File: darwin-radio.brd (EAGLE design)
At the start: 110 x 72.9 mm, 42 parts, among them J1 505110-1692, J2 505110-1692, J3 M55-6102042R, Q2 NDS8434, U1 ATWINC, U6 MCP7384X

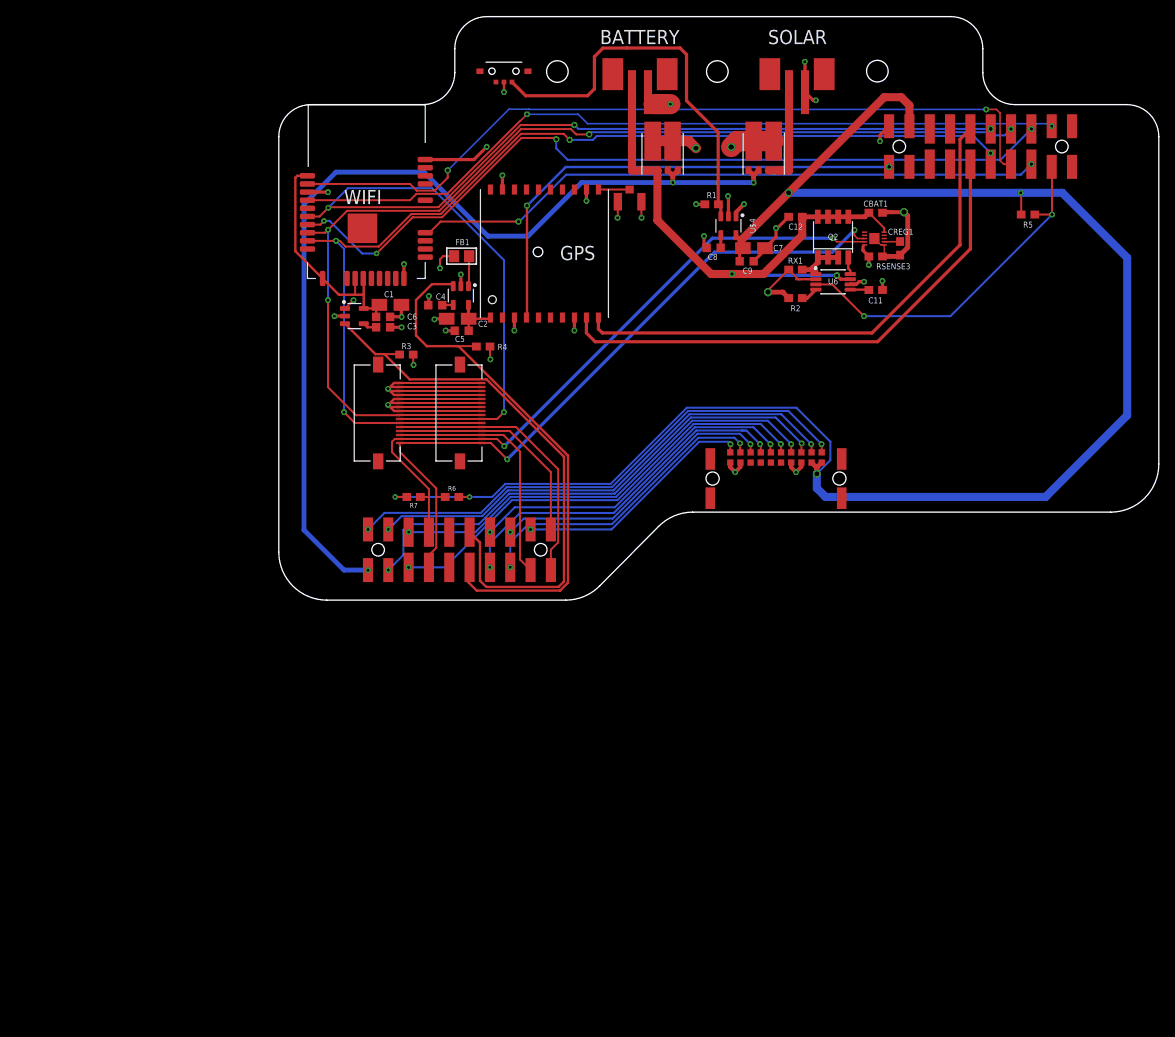
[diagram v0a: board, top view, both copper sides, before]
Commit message: Added external button header. added mounting point for single 'backpack' module. Panelized. PA1.
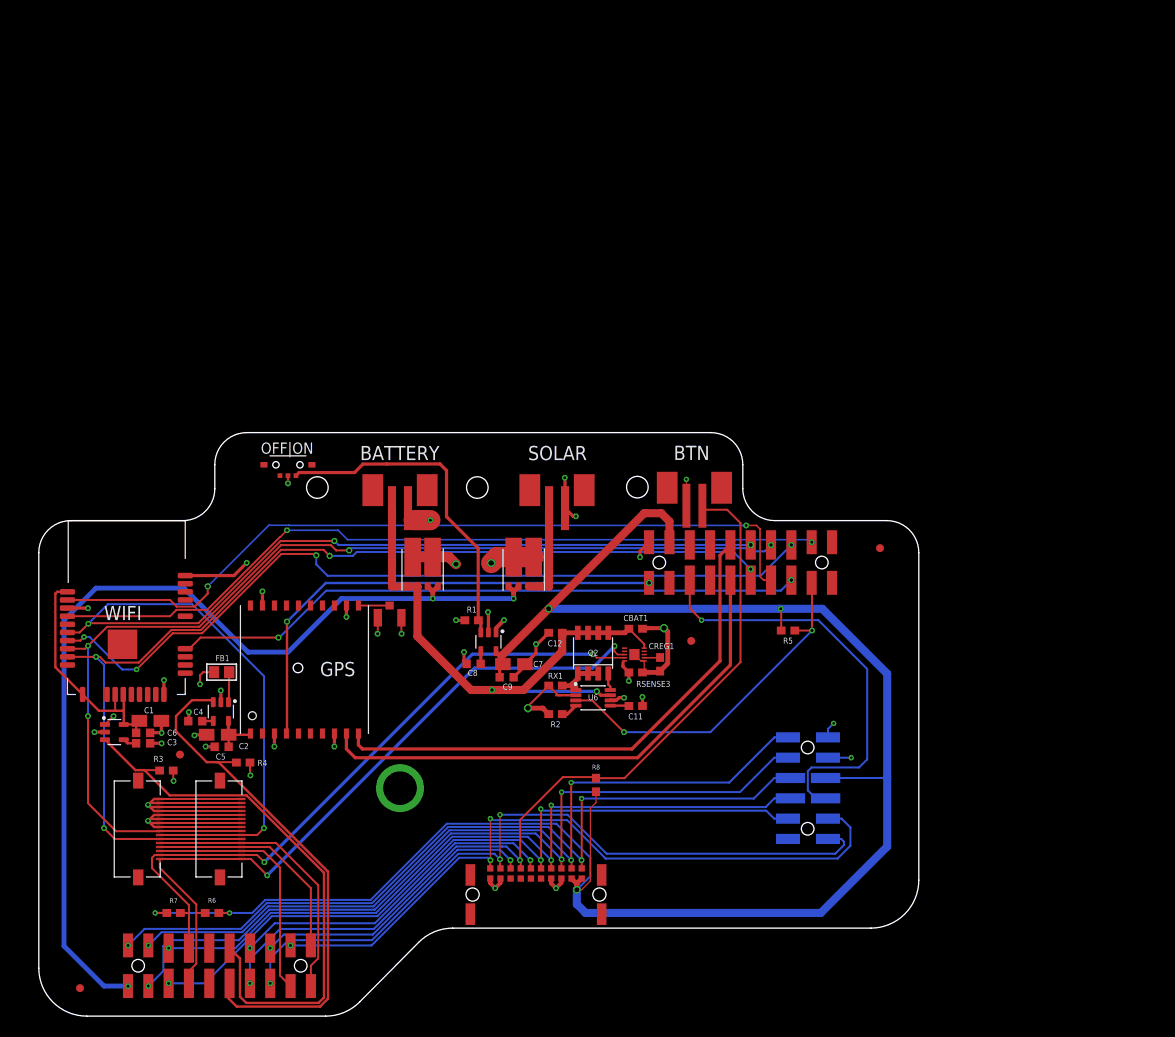
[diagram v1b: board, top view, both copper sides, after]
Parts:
- added FID1, FID2, FID3, FID4: FIDUCIAL_1MM, microbuilder:FIDUCIAL_1MM
- added R8: 100k, SparkFun-Resistors:0603
- added U$8: 2X6-HEADERSDS, Conservify:12PH
- added U$9: B2B-PH-SM4-TB, Conservify:B2B-PH-SM4-TB
- moved C12 60.0 mm to (65.4, 48.4)
- moved C7 60.0 mm to (60.2, 44.5)
- moved C9 60.0 mm to (59.3, 42.9)
- moved R6 60.0 mm to (22.5, 13.4)
- moved R7 60.0 mm to (17.7, 13.4)
- moved U$3 60.0 mm to (10.3, 36.0)
- moved U$4 60.0 mm to (57.1, 47.3)
- moved U6 60.0 mm to (70.1, 40.3)
- moved C1 60.0 mm to (14.8, 37.4)
- moved C11 60.0 mm to (75.5, 39.3)
- moved C3 60.0 mm to (13.9, 34.6)
- moved C6 60.0 mm to (13.9, 35.9)
- moved C8 60.0 mm to (55.2, 44.5)
- moved CBAT1 60.0 mm to (75.5, 48.9)
- moved D1 60.0 mm to (48.8, 53.7)
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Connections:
- net MOD_G12 renamed CHARGING
- net MOD_G3 renamed HOTSWAP_INT
- net MOD_G6 renamed GPS_ENABLE
- net MOD_G7 renamed WIFI_ENABLE
- removed net MOD_G1: J3.P1, LOWER1.PIN2
- removed net MOD_G4: J3.P4, LOWER1.PIN17
- removed net X1: UPPER1.PIN3
- new net BACKPACK_ENABLE: U$8.4, UPPER1.PIN3
- new net EEPROM_PROT: J3.P1, LOWER1.PIN2, U$8.5
- new net PIN7: U$8.7
- new net XBTN: J3.P4, LOWER1.PIN17, R8.2, U$9.-
- net 3V3: now also R8.1, U$8.3
- net GND: now also U$8.2, U$9.+
- net MOD_G2: now also U$8.6
- net MOD_MISO: now also U$8.10
- net MOD_MOSI: now also U$8.11
- net MOD_SCK: now also U$8.12
- net MOD_SCL: now also U$8.8
- net MOD_SDA: now also U$8.9
- net UNREG: now also U$8.1
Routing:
- net XBTN: track 0.00 -> 108.3 mm, vias 0 -> 2
- net EEPROM_PROT: track 0.00 -> 89.1 mm, vias 0 -> 3
- net MOD_G2: track 38.7 -> 92.3 mm, vias 2 -> 3
- net BACKPACK_ENABLE: track 0.00 -> 53.2 mm, vias 0 -> 1
- net MOD_G4: track 44.4 -> 0.00 mm, vias 2 -> 0
- net MOD_SCK: track 61.4 -> 100.6 mm, vias 2 -> 3
- net MOD_MOSI: track 63.9 -> 102.4 mm, vias 2 -> 3
- net MOD_SCL: track 56.0 -> 93.9 mm, vias 2 -> 3
- net MOD_SDA: track 55.8 -> 93.2 mm, vias 2 -> 3
- net MOD_MISO: track 65.6 -> 100.5 mm, vias 2 -> 3
- net MOD_G1: track 30.7 -> 0.00 mm, vias 2 -> 0
- net 3V3: track 220.3 -> 242.7 mm
- net N$8: track 49.7 -> 41.8 mm
- net GND: track 125.3 -> 131.5 mm, vias 30 -> 32
- net GPS_ENABLE: track 69.8 -> 67.4 mm
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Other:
- board text added: "BTN"
- board text added: "OFF|ON"

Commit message: Cleanup.
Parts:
- removed J1, J2: 505110-1692, Conservify:505110-1692
- removed J3: M55-6102042R, Conservify:M55-6102042R
- removed U$6, U$7, U$9: B2B-PH-SM4-TB, Conservify:B2B-PH-SM4-TB
- removed U$8: 2X6-HEADERSDS, Conservify:12PH
- added BACKPACK: 2X6-HEADERSDS, Conservify:12PH
- added BACKPLANE: M55-6102042R, Conservify:M55-6102042R
- added BAT-JST, BTN-JST, SOLAR-JST: B2B-PH-SM4-TB, Conservify:B2B-PH-SM4-TB
- added FFC1, FFC2: 505110-1692, Conservify:505110-1692
- C3, C4, C8: value (none) -> 470pf
- moved U$5 4.88 mm to (27.1, 68.9)
- moved FID3 0.99 mm to (81.5, 46.9)
- moved C2 0.99 mm to (22.4, 35.2)
- moved C4 0.99 mm to (19.6, 36.9)
- moved C5 0.99 mm to (22.9, 33.7)
- moved C7 0.99 mm to (59.4, 44.0)
- moved C8 0.99 mm to (54.4, 44.0)
- moved C9 0.99 mm to (58.5, 42.4)
- moved D3 0.99 mm to (60.6, 53.2)
- moved FID4 0.99 mm to (17.6, 32.7)
- moved LOWER1 0.99 mm to (34.0, 8.50)
- moved R1 0.99 mm to (54.1, 49.5)
- moved R3 0.99 mm to (15.9, 30.7)
- moved R6 0.99 mm to (21.6, 12.9)
- moved U$1 0.99 mm to (33.2, 43.3)
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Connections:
- net 3V3: now also BACKPACK.3, BACKPLANE.P11, BACKPLANE.P12; no longer J3.P11, J3.P12, U$8.3
- net BACKPACK_ENABLE: now also BACKPACK.4; no longer U$8.4
- net BAT+: now also BAT-JST.+; no longer U$7.+
- net BAT-: now also BAT-JST.-; no longer U$7.-
- net EEPROM_PROT: now also BACKPACK.5, BACKPLANE.P1; no longer J3.P1, U$8.5
- net GND: now also BACKPACK.2, BACKPLANE.P19, BACKPLANE.P20, BTN-JST.+, FFC1.1, FFC1.2, FFC1.3, FFC1.4, FFC2.1, FFC2.2, FFC2.3, FFC2.4, SOLAR-JST.-; no longer J1.1, J1.2, J1.3, J1.4, J2.1, J2.2, J2.3, J2.4, J3.P19, J3.P20, U$6.-, U$8.2, U$9.+
- net HOTSWAP_INT: now also BACKPLANE.P3; no longer J3.P3
- net MOD_G0: now also FFC1.13, FFC2.13; no longer J1.13, J2.13
- net MOD_G13: now also FFC1.14, FFC2.14; no longer J1.14, J2.14
- net MOD_G14: now also FFC1.12, FFC2.12; no longer J1.12, J2.12
- net MOD_G2: now also BACKPACK.6, BACKPLANE.P2; no longer J3.P2, U$8.6
- net MOD_G5: now also BACKPLANE.P5; no longer J3.P5
- net MOD_MISO: now also BACKPACK.10, BACKPLANE.P10; no longer J3.P10, U$8.10
- net MOD_MOSI: now also BACKPACK.11, BACKPLANE.P8; no longer J3.P8, U$8.11
- net MOD_SCK: now also BACKPACK.12, BACKPLANE.P9; no longer J3.P9, U$8.12
- net MOD_SCL: now also BACKPACK.8, BACKPLANE.P6; no longer J3.P6, U$8.8
- net MOD_SDA: now also BACKPACK.9, BACKPLANE.P7; no longer J3.P7, U$8.9
- net PIN7: now also BACKPACK.7; no longer U$8.7
- net RADIO_MISO: now also FFC1.9, FFC2.9; no longer J1.9, J2.9
- net RADIO_MOSI: now also FFC1.10, FFC2.10; no longer J1.10, J2.10
- net RADIO_SCK: now also FFC1.11, FFC2.11; no longer J1.11, J2.11
- net RAD_SCL: now also FFC1.16, FFC2.16; no longer J1.16, J2.16
- net RAD_SDA: now also FFC1.15, FFC2.15; no longer J1.15, J2.15
- net SOL+: now also SOLAR-JST.+; no longer U$6.+
- net UNREG: now also BACKPACK.1, BACKPLANE.P13, BACKPLANE.P14, FFC1.5, FFC1.6, FFC1.7, FFC1.8, FFC2.5, FFC2.6, FFC2.7, FFC2.8; no longer J1.5, J1.6, J1.7, J1.8, J2.5, J2.6, J2.7, J2.8, J3.P13, J3.P14, U$8.1
- net XBTN: now also BACKPLANE.P4, BTN-JST.-; no longer J3.P4, U$9.-
- net XX1: now also BACKPLANE.P18; no longer J3.P18
- net XX2: now also BACKPLANE.P17; no longer J3.P17
- net XX3: now also BACKPLANE.P16; no longer J3.P16
- net XX4: now also BACKPLANE.P15; no longer J3.P15
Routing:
- net N$8: track 41.8 -> 47.5 mm
- net GPS_TX: track 66.4 -> 64.5 mm
- net GPS_RX: track 65.8 -> 64.1 mm
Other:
- board size 110 x 72.9 mm -> 110 x 73 mm

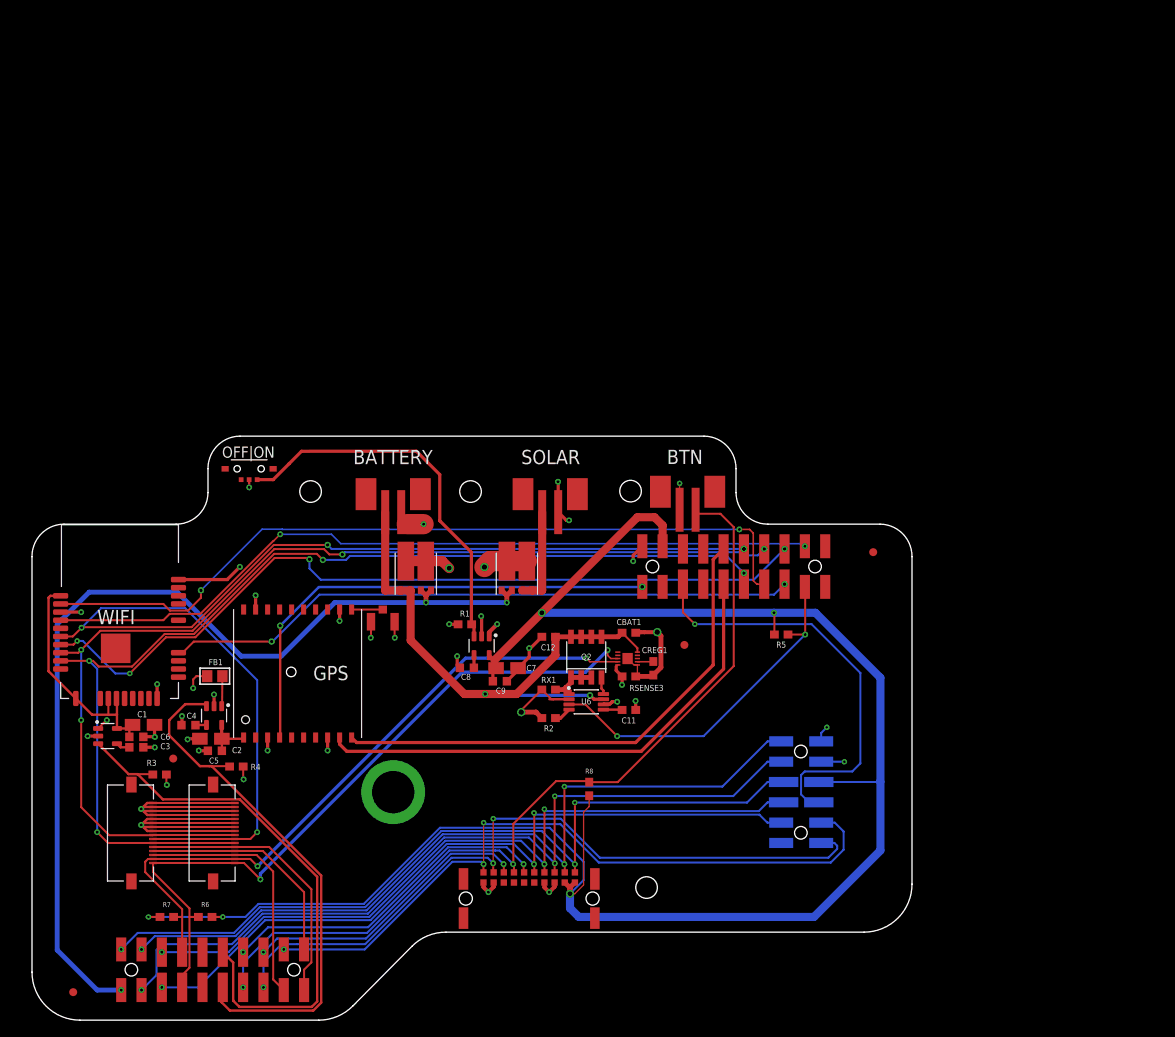
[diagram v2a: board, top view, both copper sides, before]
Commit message: Added solar pre-regulation, deprecated fuel gauge, added current sense, replaced current sense resistors, lots of routing changes, new panel.
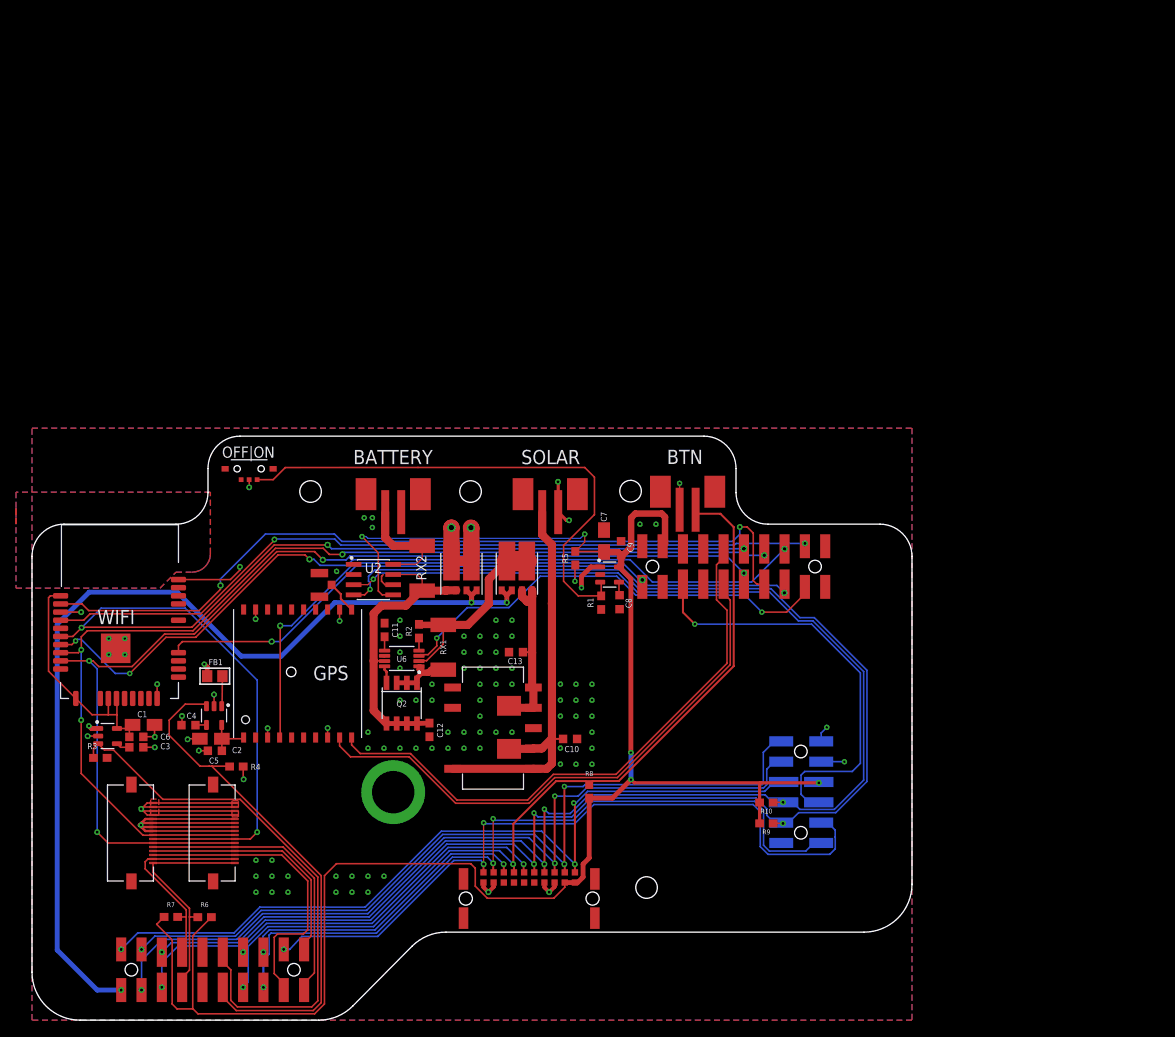
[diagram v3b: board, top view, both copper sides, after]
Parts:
- removed CBAT1: 0.1uF, SparkFun-Capacitors:0603
- removed CREG1: 10uF, SparkFun-Capacitors:0603
- removed FID1, FID2, FID3, FID4: FIDUCIAL_1MM, microbuilder:FIDUCIAL_1MM
- removed RSENSE3: 100M, SparkFun-Resistors:0603
- removed U$12: MAX17055, Conservify:10DFN-EP
- added C10, C13: 22uf, rcl:C0603K
- added J1: S1911-46R, Conservify:S1911-46R
- added R10, R9: 100k, SparkFun-Resistors:0603
- added REG1: V78E06-1000-SMT-TR, Conservify:V78E06-1000-SMT-TR
- added RX2: 100M, rcl:R2512
- added U2: INA219, Conservify:SOIC127P599X175-8N
- RX1: device SparkFun-Resistors:0603 -> rcl:R2512
- moved C11 32.1 mm to (44.1, 48.8), turned to 90 degrees
- moved R5 27.4 mm to (67.9, 57.7), turned to 270 degrees
- moved Q2 23.8 mm to (46.2, 39.6), turned to 180 degrees
- moved U6 23.7 mm to (46.2, 45.2), turned to 180 degrees
- moved C9 22.5 mm to (73.6, 59.0), turned to 90 degrees
- moved C8 20.8 mm to (73.4, 52.2), turned to 270 degrees
- moved C7 20.0 mm to (71.5, 59.9), turned to 270 degrees
- moved R2 19.5 mm to (48.4, 48.6), turned to 270 degrees
- moved C12 18.9 mm to (49.7, 36.3), turned to 270 degrees
- moved U$4 18.3 mm to (72.2, 55.7), turned to 0 degrees
- moved R1 17.3 mm to (71.1, 52.2), turned to 90 degrees
- moved RX1 14.2 mm to (51.4, 46.6), turned to 270 degrees
- moved U$11 9.16 mm to (35.9, 54.4), turned to 90 degrees
- moved R3 7.70 mm to (8.53, 32.8)
- moved D1 5.70 mm to (53.7, 53.2)
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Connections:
- removed net BAT-: BAT-JST.-, CBAT1.2, CREG1.2, RSENSE3.1, U$12.P6, U$12.PAD
- removed net N$19: CREG1.1, U$12.P7
- new net BAT+RAW: BAT-JST.+, RX2.2, U2.8
- new net SOLREG: C13.1, D3.A2-1, D3.A2-2, J1.P$1, REG1.P$4, REG1.P$5
- net 3V3: now also R10.2, R9.2, U2.5
- net BAT+: now also RX2.1, U2.7; no longer BAT-JST.+, CBAT1.1, U$12.P10
- net GND: now also BAT-JST.-, C10.2, C13.2, REG1.P$3, REG1.P$7, U1.PAD, U2.1, U2.2, U2.6; no longer RSENSE3.2, U$12.P5
- net MOD_SCL: now also R9.1, U2.4
- net MOD_SDA: now also R10.1, U2.3
- net RAD_SCL: no longer U$12.P3
- net RAD_SDA: no longer U$12.P4
- net SOL+: now also C10.1, J1.P$2, REG1.P$1, REG1.P$10, REG1.P$2; no longer D3.A2-1, D3.A2-2
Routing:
- net MOD_SCL: track 93.9 -> 198.1 mm, vias 3 -> 5
- net MOD_SDA: track 93.2 -> 190.3 mm, vias 3 -> 5
- net RAD_SCL: track 91.0 -> 29.1 mm, vias 2 -> 0
- net RAD_SDA: track 84.8 -> 26.0 mm, vias 2 -> 0
- net BAT-: track 50.7 -> 0.00 mm, vias 2 -> 0
- net SOL+: track 12.3 -> 52.0 mm
- net BAT+: track 71.3 -> 38.0 mm, vias 2 -> 0
- net CHARGESUPPLY: track 49.4 -> 26.9 mm, vias 2 -> 0
- net SOLREG: track 0.00 -> 22.5 mm
- net GND: track 131.5 -> 110.6 mm, vias 32 -> 101
- net N$8: track 47.5 -> 65.2 mm
- net CHARGING: track 44.5 -> 59.3 mm, vias 2 -> 3
- net BAT+RAW: track 0.00 -> 13.8 mm
- net 3V3: track 242.7 -> 232.1 mm
- net GPS_TX: track 64.5 -> 73.1 mm
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- added copper zone on layer 1, net GND
- added copper zone on layer 16, net GND
- added copper zone on layer 1, net GND1
